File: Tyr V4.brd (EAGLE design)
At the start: 152.4 x 115.6 mm, 190 parts, among them J1 TYR_TYR_DISPLAY, U1 TYR_ATMEGA32U4, U2 CONTROLLER_PRTR5V0U2X, U4 TYR_TPS2552, X1 CONTROLLER_USB-C-12PUSB-C-12P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, Y1 16Mhz

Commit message: Update pads
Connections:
- net GND: no longer HOLE1.P$3, HOLE2.P$3, HOLE3.P$3, HOLE4.P$3, HOLE5.P$3, HOLE6.P$3, X1.P$10, X1.P$11, X1.P$12, X1.P$7
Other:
- board text added: "JLCJLCJLC JLCJLCJLC"
- board text removed: "JLCJLCJLCJLCJLC"
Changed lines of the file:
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@@
 <rectangle x1="88.35" y1="89.05" x2="88.55" y2="89.15" layer="200"/>
 <text x="0" y="-0.5" size="0.2" layer="200" font="vector">D:/Users/Brian/Pictures/Tyr.bmp</text>
-<text x="6.25078125" y="1.271875" size="0.8" layer="22" font="vector" rot="MR0" align="center">JLCJLCJLCJLCJLC</text>
+<text x="14.2875" y="4.099609375" size="0.8" layer="22" font="vector" rot="MR0" align="center">JLCJLCJLC
+JLCJLCJLC</text>
 <wire x1="12.5015625" y1="114.839453125" x2="11.962109375" y2="114.3" width="0.001" layer="20" curve="-90"/>
 <wire x1="11.962109375" y1="114.3" x2="11.90625" y2="114.3" width="0.001" layer="20"/>
@@
 <wire x1="148.68515625" y1="108.48984375" x2="148.2328125" y2="108.9421875" width="0.1524" layer="16"/>
 <via x="148.2328125" y="108.9421875" extent="1-16" drill="0.35"/>
-<contactref element="X1" pad="P$11"/>
-<contactref element="X1" pad="P$7"/>
 <contactref element="X1" pad="P$5"/>
 <contactref element="X1" pad="P$4"/>
-<contactref element="X1" pad="P$12"/>
 <contactref element="X1" pad="P$8"/>
 <contactref element="X1" pad="P$9"/>
-<contactref element="X1" pad="P$10"/>
 <contactref element="X1" pad="P$3"/>
 <contactref element="X1" pad="P$1"/>
 <contactref element="X1" pad="P$2"/>
 <contactref element="X1" pad="P$6"/>
-<contactref element="HOLE1" pad="P$3"/>
 <contactref element="HOLE1" pad="P$1"/>
 <contactref element="HOLE1" pad="P$2"/>
-<contactref element="HOLE2" pad="P$3"/>
 <contactref element="HOLE2" pad="P$1"/>
 <contactref element="HOLE2" pad="P$2"/>
-<contactref element="HOLE3" pad="P$3"/>
 <contactref element="HOLE3" pad="P$1"/>
 <contactref element="HOLE3" pad="P$2"/>
-<contactref element="HOLE4" pad="P$3"/>
 <contactref element="HOLE4" pad="P$1"/>
 <contactref element="HOLE4" pad="P$2"/>
-<contactref element="HOLE5" pad="P$3"/>
 <contactref element="HOLE5" pad="P$1"/>
 <contactref element="HOLE5" pad="P$2"/>
-<contactref element="HOLE6" pad="P$3"/>
 <contactref element="HOLE6" pad="P$1"/>
 <contactref element="HOLE6" pad="P$2"/>
@@
 <via x="27.384375" y="1.7859375" extent="1-16" drill="0.35"/>
 <via x="83.34375" y="1.7859375" extent="1-16" drill="0.35"/>
+<wire x1="150.75" y1="95.25" x2="150.75" y2="95.25" width="0" layer="19" extent="1-16"/>
+<wire x1="150.75" y1="57.15" x2="150.75" y2="57.15" width="0" layer="19" extent="1-16"/>
+<wire x1="24.625" y1="114.04375" x2="24.625" y2="114.04375" width="0" layer="19" extent="1-16"/>
+<wire x1="136.921875" y1="1.65" x2="136.921875" y2="1.65" width="0" layer="19" extent="1-16"/>
+<wire x1="24.625" y1="110.04375" x2="24.625" y2="110.04375" width="0" layer="19" extent="1-16"/>
+<wire x1="13.475" y1="114.04375" x2="13.475" y2="114.04375" width="0" layer="19" extent="1-16"/>
+<wire x1="13.475" y1="110.04375" x2="13.475" y2="110.04375" width="0" layer="19" extent="1-16"/>
+<wire x1="1.65" y1="95.25" x2="1.65" y2="95.25" width="0" layer="19" extent="1-16"/>
+<wire x1="1.65" y1="57.15" x2="1.65" y2="57.15" width="0" layer="19" extent="1-16"/>
+<wire x1="23.8125" y1="1.65" x2="23.8125" y2="1.65" width="0" layer="19" extent="1-16"/>
 </signal>
 <signal name="VCC">
@@
 </drawing>
 <compatibility>
+<note version="6.3" minversion="6.2.2" severity="warning">
+Since Version 6.2.2 text objects can contain more than one line,
+which will not be processed correctly with this version.
+</note>
 <note version="8.3" severity="warning">
 Since Version 8.3, EAGLE supports Fusion synchronisation.

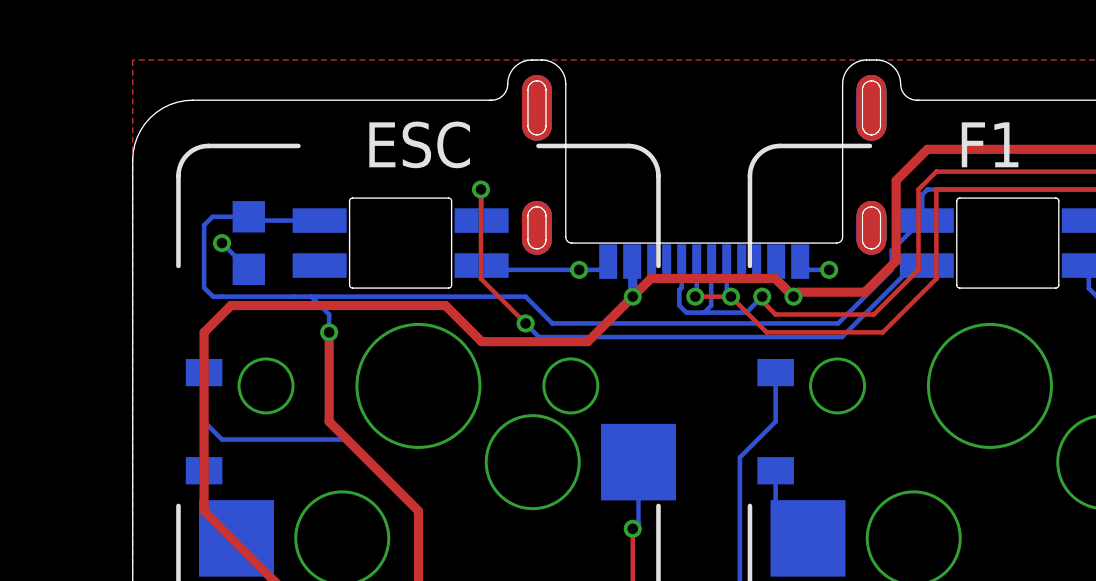
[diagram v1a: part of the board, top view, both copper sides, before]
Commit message: Added Type-C CC pulldown resistors
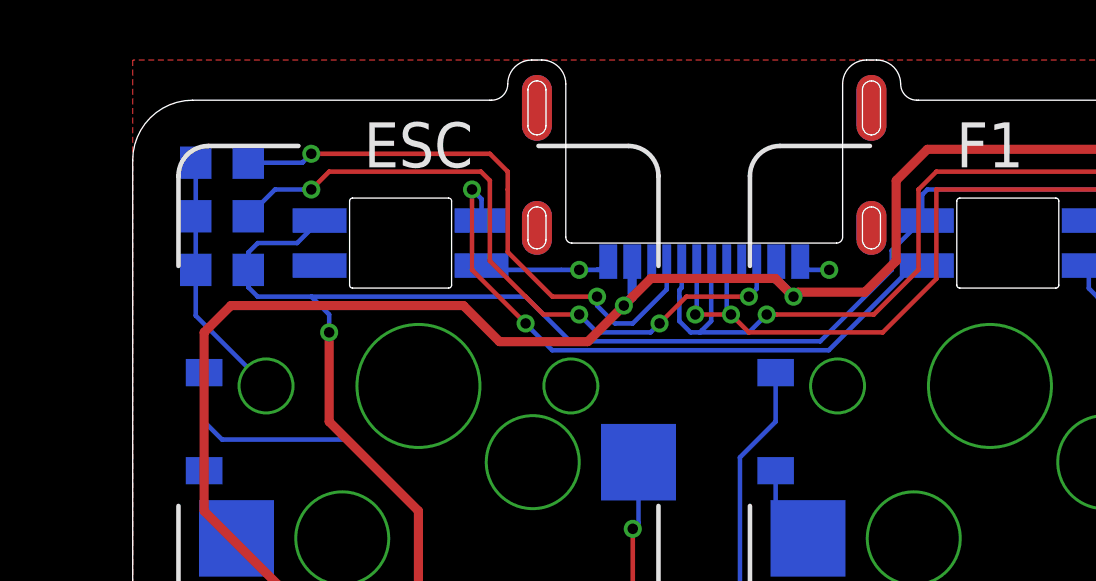
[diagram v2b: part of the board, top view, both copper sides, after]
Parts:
- added R10, R9: 5.1k, Tyr V4:COMPONENTS_R0603
- moved C10 1.26 mm to (2.98, 108.6), turned to 180 degrees
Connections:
- new net N$4: R9.1, X1.CC1
- new net N$89: R10.1, X1.CC2
- net GND: now also R10.2, R9.2
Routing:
- net N$89: track 0.00 -> 22.9 mm, vias 0 -> 4
- net N$4: track 0.00 -> 19.6 mm, vias 0 -> 2
- net GND: track 1144.9 -> 1152.1 mm, vias 62 -> 61
- net LED_VCC: track 1272.2 -> 1269.1 mm
- net N$6: track 143.5 -> 144.5 mm
- net N$7: track 142.0 -> 142.9 mm
- net N$88: track 20.7 -> 21.3 mm
